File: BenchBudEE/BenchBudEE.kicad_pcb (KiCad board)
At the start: 4 copper layers, 165.1 x 63.5 mm, 133 parts, among them K1 1461069-5, P1 24 pin Mini-fit Jr, P2 CONN_3X2, P3 CONN_2, P4 12 pin terminal block, P5 3 Pin TB, Q1 2N3904, Q2 DMN65D8L-7, Q3 B130-13-F, Q4 B130-13-F, SW1 Power Switch, U1 LTV-816S, U10 MCP4801, U2 MCP3901, U3 LMT84, U4 OPA4170, U5 AP5726, U6 LM337T, U7 LM317, U8 LM317, U9 LM337T

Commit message: Layout Work Session 6 (II)
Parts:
- moved TH5 2.16 mm to (254.3, 128.9)
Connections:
- P4 pad 8: GND_PWR -> +5V
- P4 pad 9: +5V -> GND_PWR
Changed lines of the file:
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@@
   (general
     (links 332)
-    (no_connects 295)
+    (no_connects 294)
     (area 125.171999 97.993999 290.372001 161.594001)
     (thickness 1.6)
@@
     (pad 8 thru_hole circle (at 24.5 0 90) (size 2 2) (drill 1.2)
       (layers *.Cu *.Mask F.SilkS)
-      (net 47 GND_PWR)
+      (net 6 +5V)
     )
     (pad 9 thru_hole circle (at 28 0 90) (size 2 2) (drill 1.2)
       (layers *.Cu *.Mask F.SilkS)
-      (net 6 +5V)
+      (net 47 GND_PWR)
     )
     (pad 10 thru_hole circle (at 31.5 0 90) (size 2 2) (drill 1.2)
@@
   )
   (module SM1812 (layer B.Cu)
-    (at 254.254 131.064 90)
+    (at 254.254 128.905 90)
     (tags "CMS SM")
     (attr smd)
@@
     (polygon
       (pts
-        (xy 241.935 133.35) (xy 152.146 133.35) (xy 152.146 113.538) (xy 241.935 113.538)
+        (xy 289.941 133.35) (xy 241.935 133.35) (xy 152.146 133.35) (xy 152.146 113.538) (xy 241.808 113.538)
+        (xy 241.935 113.538) (xy 284.099 113.538) (xy 284.099 112.776) (xy 289.941 112.776) (xy 289.941 113.538)
+        (xy 289.941 133.35)
       )
     )

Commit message: Layout Work Session 7
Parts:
- Q2: moved to B.Cu
- moved P2 23.7 mm to (273.3, 116.3)
- moved D5 20.2 mm to (301.1, 123.1)
- moved C10 14.6 mm to (258.6, 117.5)
- moved R45 13.4 mm to (267.5, 121.5), turned to 180 degrees
- moved R12 12.0 mm to (267.5, 116.8), turned to 180 degrees
- moved R44 11.7 mm to (267.5, 119.3), turned to 180 degrees
- moved R9 8.89 mm to (263.7, 119.3)
- moved R13 8.18 mm to (257.3, 119.8)
- moved U4 8.05 mm to (258.7, 117.5)
- moved R10 6.10 mm to (253.5, 118.5)
- moved R11 4.42 mm to (266.8, 117.3)
- moved Q2 3.42 mm to (268.2, 125.0), turned to 270 degrees
- moved P3 2.67 mm to (228.1, 120.5)
- moved 3 mm 1.53 mm to (279.7, 101.6)
- moved Q3 1.35 mm to (278.1, 130.3)
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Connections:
- P4 pad 8: +5V -> +5P
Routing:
- net N-00000125: track 52.2 -> 0.00 mm
- net /PowerAdjustmentMonitor/V-_ADJ: track 16.8 -> 0.00 mm
- net N-00000127: track 9.84 -> 0.00 mm
- net +12V: track 195.7 -> 199.7 mm
- net -12V: track 193.9 -> 197.4 mm, vias 1 -> 2
- added copper zone on F.Cu, net /Arduino/CURR_MEAS
- added copper zone on F.Cu, net /Fan/FAN_OUT-

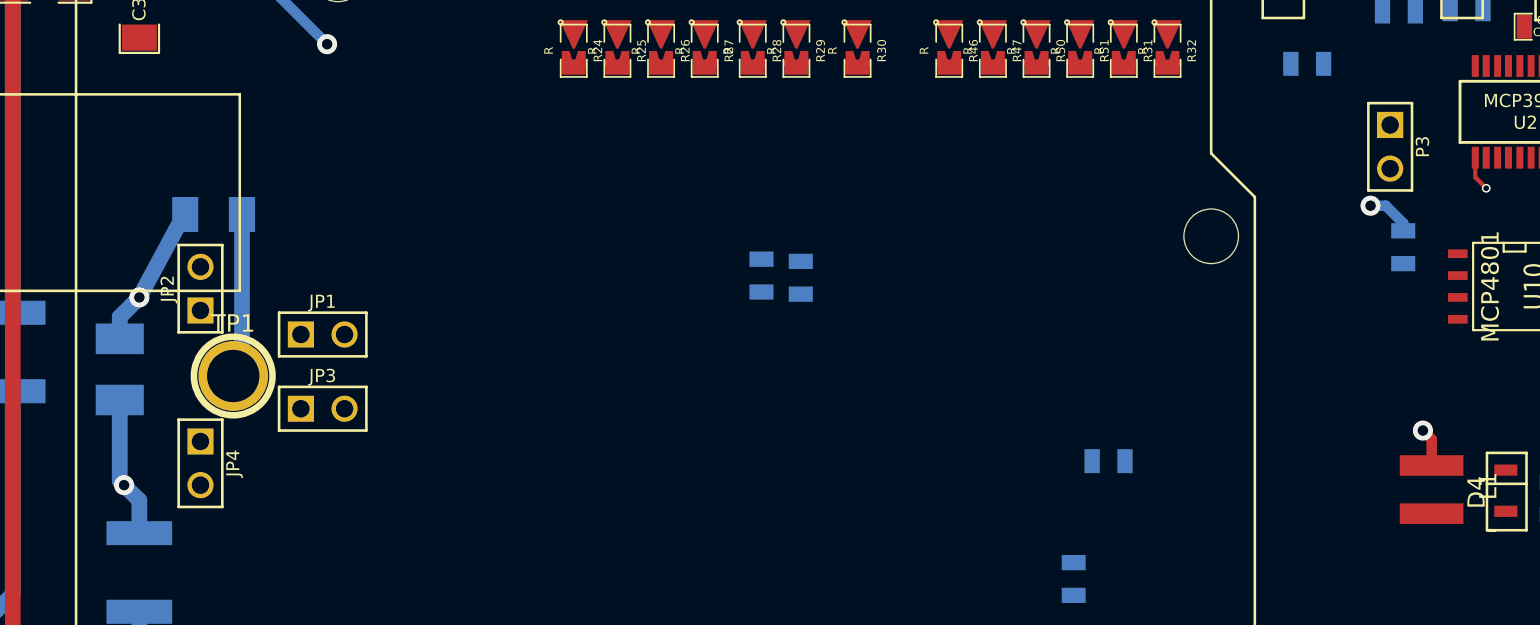
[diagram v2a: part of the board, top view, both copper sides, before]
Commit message: Connecting Ground Planes
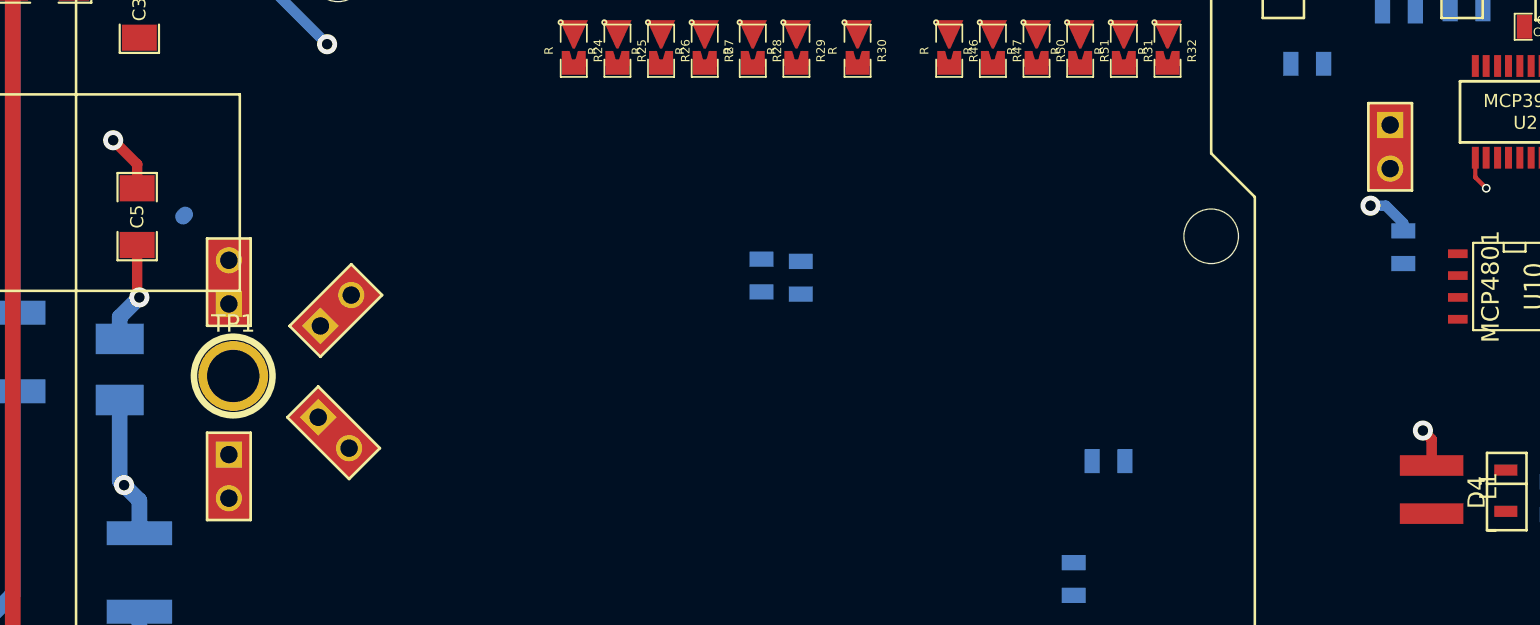
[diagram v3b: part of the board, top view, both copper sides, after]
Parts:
- C5: moved to F.Cu
- JP1, JP2, JP3, JP4, P3: footprint PIN_ARRAY_2X1 -> GND_POINT
- moved C5 4.45 mm to (155.2, 124.6), turned to 90 degrees
- moved JP4 1.82 mm to (160.5, 139.7)
- moved JP2 1.69 mm to (160.5, 128.4)
- moved JP1 1.59 mm to (166.8, 130.0), turned to 45 degrees
- moved JP3 1.53 mm to (166.6, 137.2), turned to 315 degrees
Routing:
- net GND: track 37.6 -> 43.7 mm, vias 0 -> 1
- net +5V: track 11.2 -> 8.76 mm

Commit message: Layout Work Session 8
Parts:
- R2, R5: moved to F.Cu
- R33: moved to B.Cu
- moved R33 42.6 mm to (212.6, 119.9), turned to 270 degrees
- moved R2 10.0 mm to (249.7, 148.6), turned to 0 degrees
- moved R3 9.71 mm to (253.6, 151.5), turned to 180 degrees
- moved R4 8.76 mm to (255.7, 159.3)
- moved R1 6.27 mm to (234.7, 158.6), turned to 0 degrees
- moved R6 3.09 mm to (255.4, 148.6), turned to 180 degrees
- moved R5 3.09 mm to (259.3, 151.5)
- moved Q1 2.11 mm to (261.9, 158.8), turned to 270 degrees
- moved U1 1.33 mm to (241.0, 156.1)
- moved D1 1.25 mm to (247.4, 151.9), turned to 90 degrees
- moved K1 0.38 mm to (264.5, 153.0)
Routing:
- net /Arduino/RELAY+: track 0.00 -> 56.8 mm
- net /Arduino/RELAY-: track 0.00 -> 46.5 mm
- net N-0000089: track 0.00 -> 17.7 mm
- net N-0000092: track 0.00 -> 16.1 mm
- net +12P: track 47.8 -> 62.7 mm, vias 2 -> 3
- net N-0000087: track 0.00 -> 14.1 mm, vias 0 -> 1
- net N-0000084: track 0.00 -> 12.1 mm
- net N-0000091: track 0.00 -> 6.44 mm
- net N-0000090: track 0.00 -> 5.50 mm, vias 0 -> 1
- net N-0000088: track 0.00 -> 4.41 mm
- net N-0000085: track 0.00 -> 3.66 mm
- net N-0000040: track 0.00 -> 3.37 mm
- net GND_RELAY: track 2.03 -> 3.81 mm

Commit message: Layout Work Session 9
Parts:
- moved C14 48.7 mm to (224.9, 111.5), turned to 90 degrees
- moved C22 31.5 mm to (227.5, 111.5), turned to 90 degrees
- moved C15 9.70 mm to (245.8, 111.4), turned to 270 degrees
- moved R38 8.19 mm to (251.3, 112.4)
- moved C18 7.93 mm to (230.0, 111.5), turned to 90 degrees
- moved C23 7.49 mm to (243.3, 111.4), turned to 270 degrees
- moved C16 6.10 mm to (250.7, 108.0)
- moved R41 5.99 mm to (223.8, 116.2), turned to 270 degrees
- moved C19 5.71 mm to (240.8, 111.4), turned to 270 degrees
- moved R40 3.89 mm to (230.1, 115.6), turned to 90 degrees
- moved D11 1.45 mm to (241.6, 103.9)
- moved D7 1.14 mm to (245.9, 103.9), turned to 180 degrees
- moved R37 1.02 mm to (211.7, 100.1)
- moved D6 0.97 mm to (224.4, 104.0)
- moved D10 0.38 mm to (229.7, 104.0), turned to 270 degrees
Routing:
- net /PowerAdjustmentMonitor/V+_ADJ: track 0.00 -> 91.3 mm
- net /PowerAdjustmentMonitor/V-_ADJ: track 0.00 -> 90.9 mm
- net N-00000125: track 0.00 -> 57.7 mm
- net N-00000127: track 0.00 -> 48.0 mm
- net GND_PWR: track 0.00 -> 21.9 mm, vias 0 -> 1
- net -12V: track 197.4 -> 204.6 mm
- net +12V: track 199.7 -> 205.3 mm
- net +3.3V: track 151.2 -> 151.7 mm, vias 0 -> 1

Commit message: Layout Work Session 10
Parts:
- C2: moved to F.Cu
- moved C2 39.8 mm to (279.4, 139.3), turned to 0 degrees
- moved D4 13.1 mm to (247.8, 139.7), turned to 0 degrees
- moved L1 11.4 mm to (241.8, 140.6), turned to 90 degrees
- moved C20 11.4 mm to (274.7, 106.2)
- moved C21 10.6 mm to (276.5, 106.4)
- moved C1 8.98 mm to (228.6, 139.7)
- moved R14 7.90 mm to (235.5, 136.3), turned to 180 degrees
- moved R40 7.22 mm to (223.0, 116.8)
- moved U5 6.90 mm to (233.4, 139.4), turned to 90 degrees
- moved R41 3.14 mm to (220.7, 117.0)
- moved JP4 1.65 mm to (160.5, 141.4)
- moved JP3 1.20 mm to (167.3, 138.2)
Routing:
- net +5P: track 10.5 -> 217.2 mm, vias 2 -> 3
- net /LED_Driver/LED_STRING+: track 0.00 -> 66.0 mm, vias 0 -> 2
- net /LED_Driver/LED_STRING-: track 0.00 -> 56.1 mm, vias 0 -> 2
- net N-00000120: track 0.00 -> 15.8 mm
- net GND_LED: track 1.96 -> 7.95 mm, vias 1 -> 4
- net GND: track 43.7 -> 46.8 mm
- net -12V: track 204.6 -> 205.6 mm

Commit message: Layout Work Session 11
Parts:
- added L5: INDUCTOR, SM0805, B.Cu at (234.4, 122.6)
- C2, C6, R11, U3: moved to B.Cu
- C21, C24, R42, R43, R48, R52: moved to F.Cu
- moved C13 116.7 mm to (261.4, 133.1), turned to 90 degrees
- moved C7 46.7 mm to (237.9, 122.6), turned to 180 degrees
- moved C8 37.4 mm to (230.8, 122.6), turned to 180 degrees
- moved R43 37.2 mm to (244.0, 129.4)
- moved Q3 29.3 mm to (249.0, 127.0), turned to 180 degrees
- moved TH5 28.1 mm to (281.8, 134.2)
- moved P3 22.1 mm to (206.2, 124.0)
- moved R11 21.7 mm to (247.3, 126.7), turned to 0 degrees
- moved D5 20.0 mm to (281.6, 127.0)
- moved R7 19.4 mm to (240.8, 119.9), turned to 0 degrees
- moved Q2 18.8 mm to (251.2, 117.0), turned to 180 degrees
- moved R8 17.7 mm to (247.7, 122.7), turned to 0 degrees
- moved R48 17.6 mm to (226.0, 121.3), turned to 0 degrees
- moved R9 16.0 mm to (247.7, 119.9), turned to 180 degrees
- moved R41 15.3 mm to (224.7, 131.8)
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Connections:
- C7 pad 2: +5V -> N-0000064
- P4 pad 6: /Thermocouple/TC IN - -> /Thermocouple/TC IN +
- P4 pad 7: /Thermocouple/TC IN + -> /Thermocouple/TC IN -
- U2 pad 2: +5V -> N-0000064
- U2 pad 6: /Thermocouple/CH1+ -> /Thermocouple/CH1-
- U2 pad 7: /Thermocouple/CH1- -> /Thermocouple/CH1+
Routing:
- net AGND: track 2.04 -> 123.7 mm, vias 1 -> 12
- net /Thermocouple/CH1+: track 0.00 -> 68.6 mm, vias 0 -> 1
- net /Arduino/FAN_PWM: track 0.00 -> 66.4 mm, vias 0 -> 1
- net /Thermocouple/TC IN +: track 0.00 -> 36.5 mm, vias 0 -> 1
- net /Thermocouple/TC IN -: track 0.00 -> 32.0 mm
- net /Thermocouple/CH0+: track 0.00 -> 30.9 mm, vias 0 -> 1
- net FE_V-: track 0.00 -> 29.7 mm, vias 0 -> 1
- net N-0000072: track 0.00 -> 29.7 mm, vias 0 -> 1
- net +12C: track 189.0 -> 217.9 mm
- net N-0000084: track 0.00 -> 27.9 mm, vias 0 -> 1
- net FE_V+: track 0.00 -> 27.5 mm, vias 0 -> 1
- net /Arduino/CURR_MEAS: track 0.00 -> 21.4 mm
- net N-0000083: track 0.00 -> 20.4 mm, vias 0 -> 1
- net N-00000122: track 0.00 -> 19.6 mm
- net N-0000082: track 0.00 -> 18.2 mm, vias 0 -> 2
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
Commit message: Layout Work Session 12
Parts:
- P3: footprint GND_POINT -> SM0805
- R25, R26, R28, R29, R31, R46: moved to B.Cu
- moved R38 78.8 mm to (173.2, 102.4), turned to 0 degrees
- moved R39 59.9 mm to (168.3, 102.4), turned to 0 degrees
- moved R40 58.6 mm to (168.3, 104.5), turned to 180 degrees
- moved R41 58.3 mm to (173.2, 104.5), turned to 180 degrees
- moved R15 56.7 mm to (150.1, 100.6), turned to 180 degrees
- moved R33 28.1 mm to (198.2, 143.6), turned to 180 degrees
- moved P3 19.2 mm to (224.2, 117.0)
- moved C12 13.8 mm to (230.1, 131.8)
- moved R31 12.7 mm to (199.9, 114.7), turned to 90 degrees
- moved R18 8.13 mm to (194.8, 146.3), turned to 90 degrees
- moved R17 8.06 mm to (192.3, 146.4), turned to 90 degrees
- moved C1 1.98 mm to (227.4, 140.7)
- moved L1 1.98 mm to (240.6, 141.5)
- moved D4 1.98 mm to (246.6, 140.7)
- moved R14 1.98 mm to (237.4, 140.4)
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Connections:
- ARD1 pad 1: N-0000048 -> N-0000043
- ARD1 pad 12: N-0000055 (its old number) -> (no net)
- ARD1 pad 13: N-0000047 -> N-0000048
- ARD1 pad 14: N-0000046 -> N-0000047
- ARD1 pad 15: N-0000033 -> N-0000032
- ARD1 pad 16: N-0000045 -> N-0000046
- ARD1 pad 17: (no net) -> N-0000037
- ARD1 pad 21: N-0000034 -> N-0000041
- ARD1 pad 22: N-0000060 -> N-0000035
- ARD1 pad 23: N-0000035 -> N-0000060
- ARD1 pad 3: N-0000041 -> N-0000050
- R16 pad 1: +5V -> N-0000043
- R16 pad 2: N-0000048 -> +5V
- R17 pad 1: GND -> N-0000049
- R17 pad 2: N-0000049 -> GND
- R18 pad 1: GND -> N-0000050
- R18 pad 2: N-0000041 -> GND
- R19 pad 1: +12P -> N-0000040
- R19 pad 2: N-0000040 -> +12P
- R24 pad 1: N-0000061 -> /Arduino/SCLK
- R24 pad 2: /Arduino/SCLK -> N-0000061
- R25 pad 1: N-0000035 -> /Arduino/MOSI
- R25 pad 2: /Arduino/MISO -> N-0000060
- R26 pad 1: N-0000060 -> /Arduino/MISO
- R26 pad 2: /Arduino/MOSI -> N-0000035
- R27 pad 1: N-0000034 -> /Arduino/FAN_PWM
- R27 pad 2: /Arduino/FAN_PWM -> N-0000041
- R28 pad 1: N-0000056 -> /Arduino/LED_EN_PWM
- R28 pad 2: /Arduino/LED_EN_PWM -> N-0000056
- R29 pad 1: N-0000057 -> /Arduino/~ADC_CS
- R29 pad 2: /Arduino/~ADC_CS -> N-0000057
- R30 pad 1: N-0000059 -> /Fan/CS_N
- R30 pad 2: /Fan/CS_N -> N-0000059
- R31 pad 1: N-0000055 (its old number) -> /Arduino/RELAY+
- R31 pad 2: /Arduino/RELAY+ -> N-0000037
- R32 pad 1: N-0000058 -> /Arduino/FAN_MODE
- R32 pad 2: /Arduino/FAN_MODE -> N-0000058
- R33 pad 1: GND -> /Arduino/RELAY-
- R33 pad 2: /Arduino/RELAY- -> GND
- R46 pad 1: N-0000045 -> /Arduino/~RESET
- R46 pad 2: /Arduino/~RESET -> N-0000046
- R47 pad 1: N-0000033 -> /Arduino/~DR
- R47 pad 2: /Arduino/~DR -> N-0000032
- R50 pad 1: N-0000046 -> /Arduino/~LDAC
- R50 pad 2: /Arduino/~LDAC -> N-0000047
- R51 pad 1: N-0000047 -> /Fan/~SDHN
- R51 pad 2: /Fan/~SDHN -> N-0000048
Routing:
- net /Fan/TACH_IN: track 0.00 -> 98.3 mm
- net GND: track 46.8 -> 119.4 mm, vias 1 -> 4
- net /Arduino/MOSI: track 0.00 -> 72.4 mm, vias 0 -> 1
- net /Arduino/V+_ADJ_MON: track 0.00 -> 71.6 mm, vias 0 -> 1
- net /Arduino/SCLK: track 0.00 -> 69.9 mm, vias 0 -> 2
- net /Arduino/V-_ADJ_MON: track 0.00 -> 68.8 mm, vias 0 -> 1
- net N-00000108: track 0.00 -> 62.0 mm
- net /Arduino/MISO: track 0.00 -> 60.2 mm, vias 0 -> 1
- net /Arduino/LED_EN_PWM: track 0.00 -> 58.3 mm, vias 0 -> 1
- net /PowerAdjustmentMonitor/V-_ADJ: track 90.9 -> 147.7 mm
- net /Arduino/CURR_MEAS: track 21.4 -> 77.1 mm
- net /PowerAdjustmentMonitor/V+_ADJ: track 91.3 -> 143.1 mm, vias 0 -> 1
- net /Arduino/~RESET: track 0.00 -> 49.8 mm, vias 0 -> 1
- net /Arduino/~ADC_CS: track 0.00 -> 45.7 mm, vias 0 -> 1
- net /Arduino/FAN_MODE: track 0.00 -> 45.0 mm, vias 0 -> 2
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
